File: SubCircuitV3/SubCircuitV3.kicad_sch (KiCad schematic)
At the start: 23 parts, among them J1 JTAG, J10 ESC_POWER, J11 ESC_POWER, J12 ESC_POWER, J13 ESC_POWER, J14 FEMALE XT-60, J15 ESC PWM, J16 3S, J2 ESC PWM, J3 ESC PWM, J4 ESC PWM, J5 ESC PWM, J6 ESC PWM, J7 5S, J8 ESC_POWER, J9 ESC_POWER, K1 G5Q-1A

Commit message: Finalized V3 Board
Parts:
- added R3: 1000, Resistor_THT:R_Axial_DIN0207_L6.3mm_D2.5mm_P10.16mm_Horizontal, symbol Device:R
- R1: value 2000 -> 1000
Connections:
- net +12V: now also R1.2, R3.2; no longer R1.1
- net at K1.1: now also R1.1, R3.1; no longer R1.2
- net at C1.1, CR1.3 (INPUT), K1.3: no longer J1.14 (Pin_14)
- net at C2.1, CR1.2 (OUTPUT), J14.1 (Pin_1): now also J1.14 (Pin_14)
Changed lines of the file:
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@@
   (junction (at 247.65 95.25) (diameter 0) (color 0 0 0 0)
   )
-  (junction (at 170.18 95.25) (diameter 0) (color 0 0 0 0)
-  )
   (junction (at 104.14 137.16) (diameter 0) (color 0 0 0 0)
   )
@@
   (junction (at 170.18 115.57) (diameter 0) (color 0 0 0 0)
   )
+  (junction (at 247.65 82.55) (diameter 0) (color 0 0 0 0)
+  )
   (junction (at 243.84 102.87) (diameter 0) (color 0 0 0 0)
+  )
+  (junction (at 160.02 120.65) (diameter 0) (color 0 0 0 0)
+  )
+  (junction (at 154.94 113.03) (diameter 0) (color 0 0 0 0)
   )
   (junction (at 187.96 95.25) (diameter 0) (color 0 0 0 0)
@@
   (no_connect (at 96.52 107.95))
   (no_connect (at 97.79 93.98))
+  (wire (pts (xy 151.13 113.03) (xy 154.94 113.03))
+    (stroke (width 0) (type default))
+  )
   (wire (pts (xy 109.22 77.47) (xy 109.22 124.46))
     (stroke (width 0) (type default))
@@
     (stroke (width 0) (type default))
   )
-  (wire (pts (xy 160.02 113.03) (xy 154.94 113.03))
-    (stroke (width 0) (type default))
-  )
   (wire (pts (xy 116.84 124.46) (xy 142.24 124.46))
     (stroke (width 0) (type default))
@@
     (stroke (width 0) (type default))
   )
-  (wire (pts (xy 170.18 81.28) (xy 170.18 95.25))
-    (stroke (width 0) (type default))
-  )
   (wire (pts (xy 111.76 91.44) (xy 111.76 124.46))
     (stroke (width 0) (type default))
@@
     (stroke (width 0) (type default))
   )
-  (wire (pts (xy 142.24 81.28) (xy 170.18 81.28))
+  (wire (pts (xy 142.24 81.28) (xy 247.65 81.28))
     (stroke (width 0) (type default))
   )
@@
     (stroke (width 0) (type default))
   )
+  (wire (pts (xy 154.94 113.03) (xy 160.02 113.03))
+    (stroke (width 0) (type default))
+  )
   (wire (pts (xy 242.57 95.25) (xy 247.65 95.25))
     (stroke (width 0) (type default))
@@
     (stroke (width 0) (type default))
   )
+  (wire (pts (xy 247.65 81.28) (xy 247.65 82.55))
+    (stroke (width 0) (type default))
+  )
   (wire (pts (xy 97.79 91.44) (xy 104.14 91.44))
     (stroke (width 0) (type default))
@@
   )
   (wire (pts (xy 106.68 137.16) (xy 107.95 137.16))
+    (stroke (width 0) (type default))
+  )
+  (wire (pts (xy 151.13 120.65) (xy 160.02 120.65))
     (stroke (width 0) (type default))
   )
@@
     (effects (font (size 1.27 1.27)) (justify left top))
   )
-  (symbol (lib_id "power:PWR_FLAG") (at 170.18 115.57 270) (unit 1)
-    (in_bom yes) (on_board yes) (dnp no) (fields_autoplaced)
-    (property "Reference" "#FLG02" (at 172.085 115.57 0)
-      (effects (font (size 1.27 1.27)) hide)
-    )
-    (property "Value" "PWR_FLAG" (at 173.99 115.57 90)
+  (symbol (lib_id "power:PWR_FLAG") (at 170.18 115.57 0) (unit 1)
+    (in_bom yes) (on_board yes) (dnp no)
+    (property "Reference" "#FLG02" (at 170.18 113.665 0)
+      (effects (font (size 1.27 1.27)) hide)
+    )
+    (property "Value" "PWR_FLAG" (at 170.18 111.76 0)
       (effects (font (size 1.27 1.27)) (justify left))
     )
@@
     )
   )
-  (symbol (lib_id "Device:R") (at 160.02 116.84 180) (unit 1)
+  (symbol (lib_id "power:+7.5V") (at 170.18 120.65 180) (unit 1)
     (in_bom yes) (on_board yes) (dnp no)
-    (property "Reference" "R1" (at 153.67 116.84 90)
-      (effects (font (size 1.27 1.27)))
-    )
-    (property "Value" "2000" (at 156.21 116.84 90)
-      (effects (font (size 1.27 1.27)))
-    )
-    (property "Footprint" "Resistor_THT:R_Axial_DIN0207_L6.3mm_D2.5mm_P10.16mm_Horizontal" (at 161.798 116.84 90)
-      (effects (font (size 1.27 1.27)) hide)
-    )
-    (property "Datasheet" "~" (at 160.02 116.84 0)
-      (effects (font (size 1.27 1.27)) hide)
-    )
-    (pin "1")
-    (pin "2")
-    (instances
-      (project "SubCircuitV3"
-        (path "/364d75d3-77e7-4f3e-a207-f79712f2b174"
-          (reference "R1") (unit 1)
-        )
-      )
-    )
-  )
-  (symbol (lib_id "power:+7.5V") (at 170.18 120.65 180) (unit 1)
-    (in_bom yes) (on_board yes) (dnp no) (fields_autoplaced)
     (property "Reference" "#PWR010" (at 170.18 116.84 0)
       (effects (font (size 1.27 1.27)) hide)
@@
         (path "/364d75d3-77e7-4f3e-a207-f79712f2b174"
           (reference "#PWR09") (unit 1)
+        )
+      )
+    )
+  )
+  (symbol (lib_id "Device:R") (at 160.02 116.84 0) (unit 1)
+    (in_bom yes) (on_board yes) (dnp no) (fields_autoplaced)
+    (property "Reference" "R3" (at 162.56 115.57 0)
+      (effects (font (size 1.27 1.27)) (justify left))
+    )
+    (property "Value" "1000" (at 162.56 118.11 0)
+      (effects (font (size 1.27 1.27)) (justify left))
+    )
+    (property "Footprint" "Resistor_THT:R_Axial_DIN0207_L6.3mm_D2.5mm_P10.16mm_Horizontal" (at 158.242 116.84 90)
+      (effects (font (size 1.27 1.27)) hide)
+    )
+    (property "Datasheet" "~" (at 160.02 116.84 0)
+      (effects (font (size 1.27 1.27)) hide)
+    )
+    (pin "1")
+    (pin "2")
+    (instances
+      (project "SubCircuitV3"
+        (path "/364d75d3-77e7-4f3e-a207-f79712f2b174"
+          (reference "R3") (unit 1)
         )
       )
@@
         )
       )
+    )
+  )
+  (symbol (lib_id "Device:R") (at 151.13 116.84 0) (unit 1)
+    (in_bom yes) (on_board yes) (dnp no) (fields_autoplaced)
+    (property "Reference" "R1" (at 153.67 115.57 0)
+      (effects (font (size 1.27 1.27)) (justify left))
+    )
+    (property "Value" "1000" (at 153.67 118.11 0)
+      (effects (font (size 1.27 1.27)) (justify left))
+    )
+    (property "Footprint" "Resistor_THT:R_Axial_DIN0207_L6.3mm_D2.5mm_P10.16mm_Horizontal" (at 149.352 116.84 90)
+      (effects (font (size 1.27 1.27)) hide)
+    )
+    (property "Datasheet" "~" (at 151.13 116.84 0)
+      (effects (font (size 1.27 1.27)) hide)
+    )
+    (pin "1")
+    (pin "2")
+    (instances
+      (project "SubCircuitV3"
+        (path "/364d75d3-77e7-4f3e-a207-f79712f2b174"
+          (reference "R1") (unit 1)
+        )
+      )

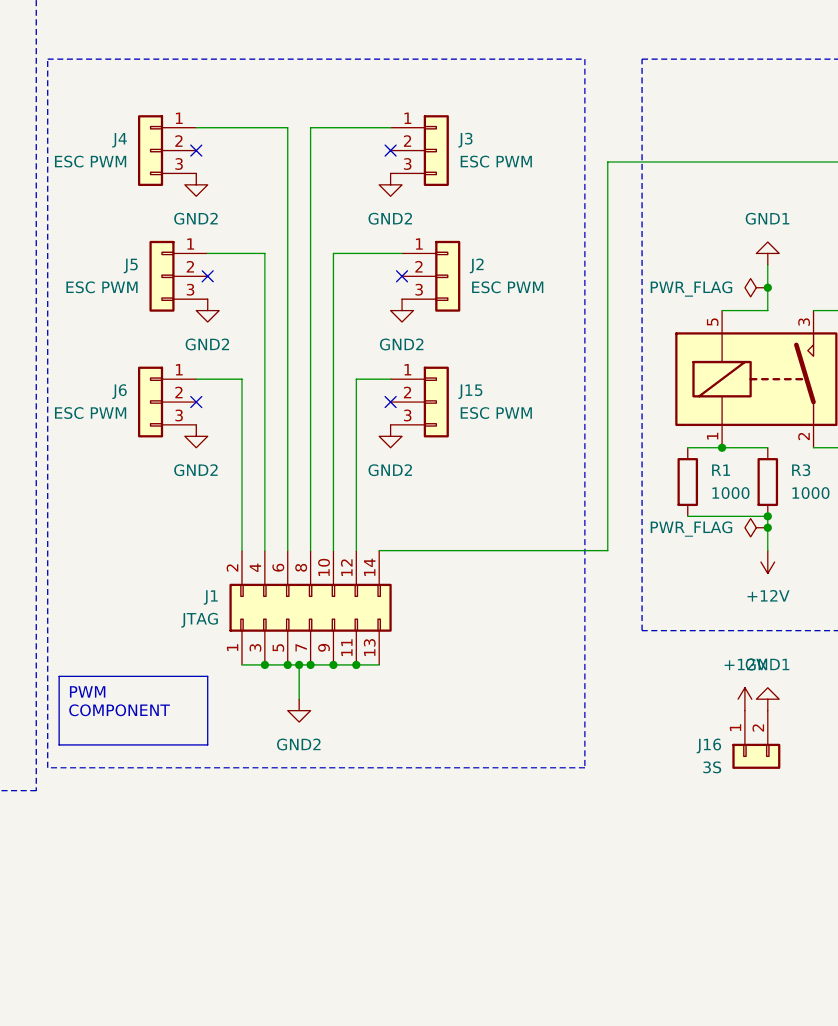
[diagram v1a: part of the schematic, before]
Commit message: Added water sensors and fixed JTAG-Capacitor connection error
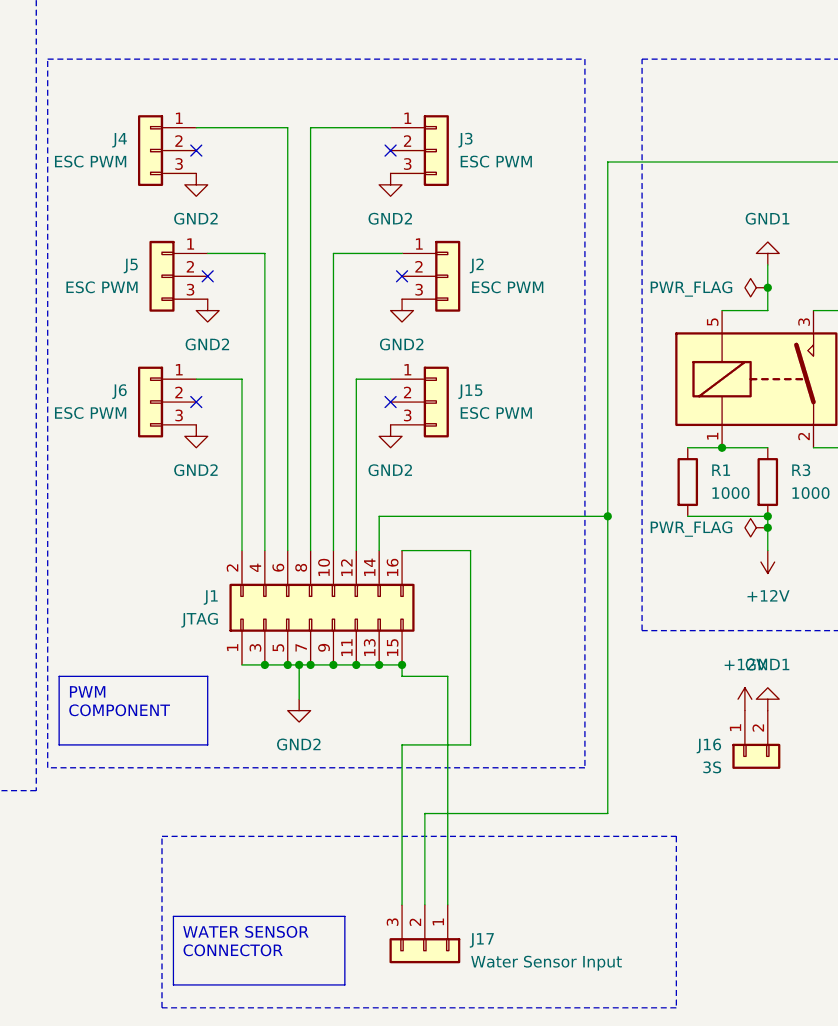
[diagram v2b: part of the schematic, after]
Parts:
- removed J1: JTAG, Connector_PinHeader_2.00mm:PinHeader_2x07_P2.00mm_Vertical, symbol Connector_Generic:Conn_02x07_Odd_Even
- added J1: JTAG, Connector_PinHeader_2.00mm:PinHeader_2x08_P2.00mm_Vertical, symbol Connector_Generic:Conn_02x08_Odd_Even
- added J17: Water Sensor Input, Connector_PinHeader_2.00mm:PinHeader_1x03_P2.00mm_Vertical, symbol Connector_Generic:Conn_01x03
- CR1: footprint LD1085V50_footprints:TO-220_STM -> TO-220_STM
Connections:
- net GND2: now also J1.1 (Pin_1), J1.11 (Pin_11), J1.13 (Pin_13), J1.15 (Pin_15), J1.3 (Pin_3), J1.5 (Pin_5), J1.7 (Pin_7), J1.9 (Pin_9), J17.1 (Pin_1)
- net at C2.1, CR1.2 (OUTPUT), J14.1 (Pin_1): now also J1.14 (Pin_14), J17.2 (Pin_2)
- net at J5.1 (Pin_1): now also J1.4 (Pin_4)
- net at J2.1 (Pin_1): now also J1.10 (Pin_10)
- net at J15.1 (Pin_1): now also J1.12 (Pin_12)
- net at J6.1 (Pin_1): now also J1.2 (Pin_2)
- net at J4.1 (Pin_1): now also J1.6 (Pin_6)
- net at J3.1 (Pin_1): now also J1.8 (Pin_8)
- new net: J1.16 (Pin_16), J17.3 (Pin_3)

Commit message: Killswitch and MOSFET implementation
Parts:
- added J18: XLR3_Switched, symbol Connector_Audio:XLR3_Switched
- added Q1, Q2, Q3, Q4, Q5, Q6: NMOS, symbol Simulation_SPICE:NMOS
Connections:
- net +12V: now also J18.N, Q1.1 (D), Q2.1 (D), Q3.1 (D), Q4.1 (D), Q5.1 (D), Q6.1 (D); no longer J10.2 (Pin_2), J11.2 (Pin_2), J12.2 (Pin_2), J13.2 (Pin_2), J8.2 (Pin_2), J9.2 (Pin_2), R1.2, R3.2
- new net: J12.2 (Pin_2), Q5.3 (S)
- new net: J10.2 (Pin_2), Q3.3 (S)
- new net: J11.2 (Pin_2), Q4.3 (S)
- new net: J9.2 (Pin_2), Q2.3 (S)
- new net: J8.2 (Pin_2), Q1.3 (S)
- new net: J13.2 (Pin_2), Q6.3 (S)
- new net SG: J18.NO, Q1.2 (G), Q2.2 (G), Q3.2 (G), Q4.2 (G), Q5.2 (G), Q6.2 (G), R1.2, R3.2
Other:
- moved on the sheet: D1, J10, J11, J12, J13, J8, J9, R2

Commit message: Fixed custom footprint assignments
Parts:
- C1, C2: footprint 860010372001:CAP_WCAP-ATG8_5x11_WRE -> Capacitor_WCAP-ATG8_5x11_WRE:CAP_WCAP-ATG8_5x11_WRE
- CR1: footprint TO-220_STM -> LD1085V50_footprints:TO-220_STM
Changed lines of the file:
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@@
       (effects (font (size 1.27 1.27)) (justify left))
     )
-    (property "Footprint" "860010372001:CAP_WCAP-ATG8_5x11_WRE" (at 248.6152 102.87 0)
+    (property "Footprint" "Capacitor_WCAP-ATG8_5x11_WRE:CAP_WCAP-ATG8_5x11_WRE" (at 248.6152 102.87 0)
       (effects (font (size 1.27 1.27)) hide)
     )
@@
       (effects (font (size 1.27 1.27)) (justify left))
     )
-    (property "Footprint" "860010372001:CAP_WCAP-ATG8_5x11_WRE" (at 188.9252 102.87 0)
+    (property "Footprint" "Capacitor_WCAP-ATG8_5x11_WRE:CAP_WCAP-ATG8_5x11_WRE" (at 188.9252 102.87 0)
       (effects (font (size 1.27 1.27)) hide)
     )
@@
       (effects (font (size 1.524 1.524)))
     )
-    (property "Footprint" "TO-220_STM" (at 242.57 92.71 0)
+    (property "Footprint" "LD1085V50_footprints:TO-220_STM" (at 242.57 92.71 0)
       (effects (font (size 1.27 1.27) italic) hide)
     )

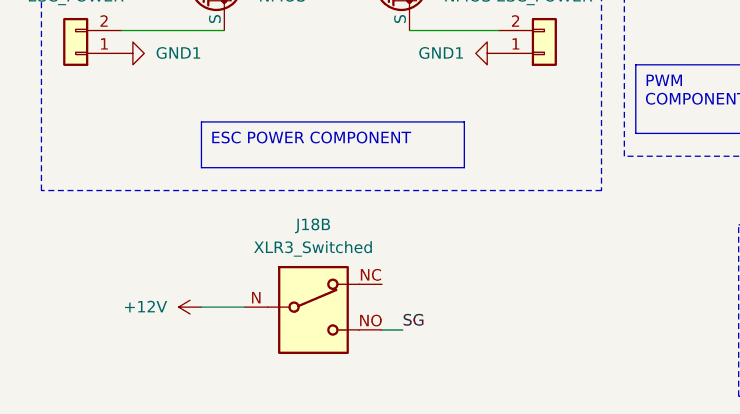
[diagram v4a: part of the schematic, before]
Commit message: Added mosfet
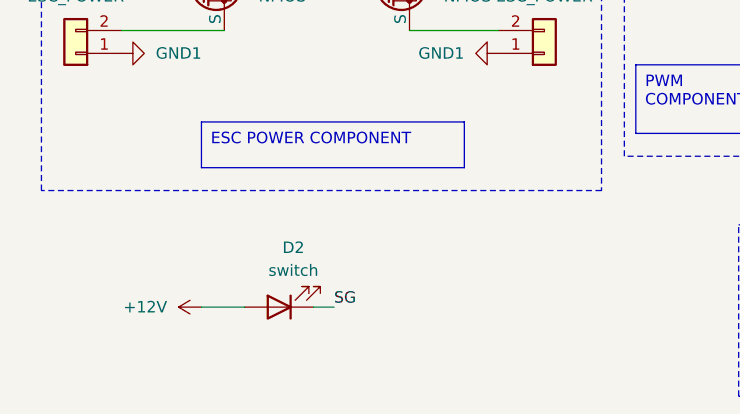
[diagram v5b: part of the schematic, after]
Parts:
- removed J18: XLR3_Switched, symbol Connector_Audio:XLR3_Switched
- added D2: switch, LED_THT:LED_D5.0mm_Horizontal_O6.35mm_Z9.0mm, symbol Device:LED
- CR1: footprint LD1085V50_footprints:TO-220_STM -> LD1085V50:TO-220_STM
- Q1, Q2, Q3, Q4, Q5, Q6: footprint (none) -> BSZ065N03LSATMA1-MOSFET:BSZ065N03LSATMA1
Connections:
- net +12V: now also D2.2 (A)
- net SG: now also D2.1 (K)
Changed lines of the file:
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@@
     (stroke (width 0) (type default))
   )
-  (wire (pts (xy 53.086 167.894) (xy 55.372 167.894))
+  (wire (pts (xy 45.466 165.354) (xy 47.752 165.354))
     (stroke (width 0) (type default))
   )
@@
     (effects (font (size 1.27 1.27)) (justify left bottom))
   )
-  (label "SG" (at 55.372 167.894 0) (fields_autoplaced)
+  (label "SG" (at 47.752 165.354 0) (fields_autoplaced)
     (effects (font (size 1.27 1.27)) (justify left bottom))
   )
@@
       (effects (font (size 1.27 1.27)) (justify left))
     )
-    (property "Footprint" "" (at 58.674 113.03 0)
+    (property "Footprint" "BSZ065N03LSATMA1-MOSFET:BSZ065N03LSATMA1" (at 58.674 113.03 0)
       (effects (font (size 1.27 1.27)) hide)
     )
@@
       (effects (font (size 1.27 1.27)) (justify left))
     )
-    (property "Footprint" "" (at 38.1 127 0)
+    (property "Footprint" "BSZ065N03LSATMA1-MOSFET:BSZ065N03LSATMA1" (at 38.1 127 0)
       (effects (font (size 1.27 1.27)) hide)
     )
@@
       (effects (font (size 1.524 1.524)))
     )
-    (property "Footprint" "LD1085V50_footprints:TO-220_STM" (at 242.57 92.71 0)
+    (property "Footprint" "LD1085V50:TO-220_STM" (at 242.57 92.71 0)
       (effects (font (size 1.27 1.27) italic) hide)
     )
@@
       (effects (font (size 1.27 1.27)) (justify left))
     )
-    (property "Footprint" "" (at 58.928 97.79 0)
+    (property "Footprint" "BSZ065N03LSATMA1-MOSFET:BSZ065N03LSATMA1" (at 58.928 97.79 0)
       (effects (font (size 1.27 1.27)) hide)
     )
@@
       (effects (font (size 1.27 1.27)) (justify left))
     )
-    (property "Footprint" "" (at 38.1 113.03 0)
+    (property "Footprint" "BSZ065N03LSATMA1-MOSFET:BSZ065N03LSATMA1" (at 38.1 113.03 0)
       (effects (font (size 1.27 1.27)) hide)
     )
@@
       (effects (font (size 1.27 1.27)) (justify left))
     )
-    (property "Footprint" "" (at 38.1 97.79 0)
+    (property "Footprint" "BSZ065N03LSATMA1-MOSFET:BSZ065N03LSATMA1" (at 38.1 97.79 0)
       (effects (font (size 1.27 1.27)) hide)
     )
@@
       (effects (font (size 1.27 1.27)) (justify left))
     )
-    (property "Footprint" "" (at 58.674 127 0)
+    (property "Footprint" "BSZ065N03LSATMA1-MOSFET:BSZ065N03LSATMA1" (at 58.674 127 0)
       (effects (font (size 1.27 1.27)) hide)
     )
@@
     )
   )
+  (symbol (lib_id "Device:LED") (at 41.656 165.354 180) (unit 1)
+    (in_bom yes) (on_board yes) (dnp no) (fields_autoplaced)
+    (property "Reference" "D2" (at 43.2435 158.75 0)
+      (effects (font (size 1.27 1.27)))
+    )
+    (property "Value" "switch" (at 43.2435 161.29 0)
+      (effects (font (size 1.27 1.27)))
+    )
+    (property "Footprint" "LED_THT:LED_D5.0mm_Horizontal_O6.35mm_Z9.0mm" (at 41.656 165.354 0)
+      (effects (font (size 1.27 1.27)) hide)
+    )
+    (property "Datasheet" "~" (at 41.656 165.354 0)
+      (effects (font (size 1.27 1.27)) hide)
+    )
+    (pin "1")
+    (pin "2")
+    (instances
+      (project "SubCircuitV3"
+        (path "/364d75d3-77e7-4f3e-a207-f79712f2b174"
+          (reference "D2") (unit 1)
+        )
+      )
+    )
+  )
   (symbol (lib_id "Device:R") (at 151.13 116.84 0) (unit 1)
     (in_bom yes) (on_board yes) (dnp no) (fields_autoplaced)
@@
         )
       )
-    )
-  )
-  (symbol (lib_id "Connector_Audio:XLR3_Switched") (at 45.466 165.354 0) (unit 2)
-    (in_bom yes) (on_board yes) (dnp no) (fields_autoplaced)
-    (property "Reference" "J18" (at 45.466 156.21 0)
-      (effects (font (size 1.27 1.27)))
-    )
-    (property "Value" "XLR3_Switched" (at 45.466 158.75 0)
-      (effects (font (size 1.27 1.27)))
-    )
-    (property "Footprint" "" (at 45.466 162.814 0)
-      (effects (font (size 1.27 1.27)) hide)
-    )
-    (property "Datasheet" " ~" (at 45.466 162.814 0)
-      (effects (font (size 1.27 1.27)) hide)
-    )
-    (pin "1")
-    (pin "2")
-    (pin "3")
-    (pin "N")
-    (pin "NC")
-    (pin "NO")
-    (instances
-      (project "SubCircuitV3"
-        (path "/364d75d3-77e7-4f3e-a207-f79712f2b174"
-          (reference "J18") (unit 2)
-        )
-      )
